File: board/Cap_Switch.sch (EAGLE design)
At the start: 9 parts, among them K1 TOS TLP241A, Q1 PN2222ABU, Q2 PN2222ABU

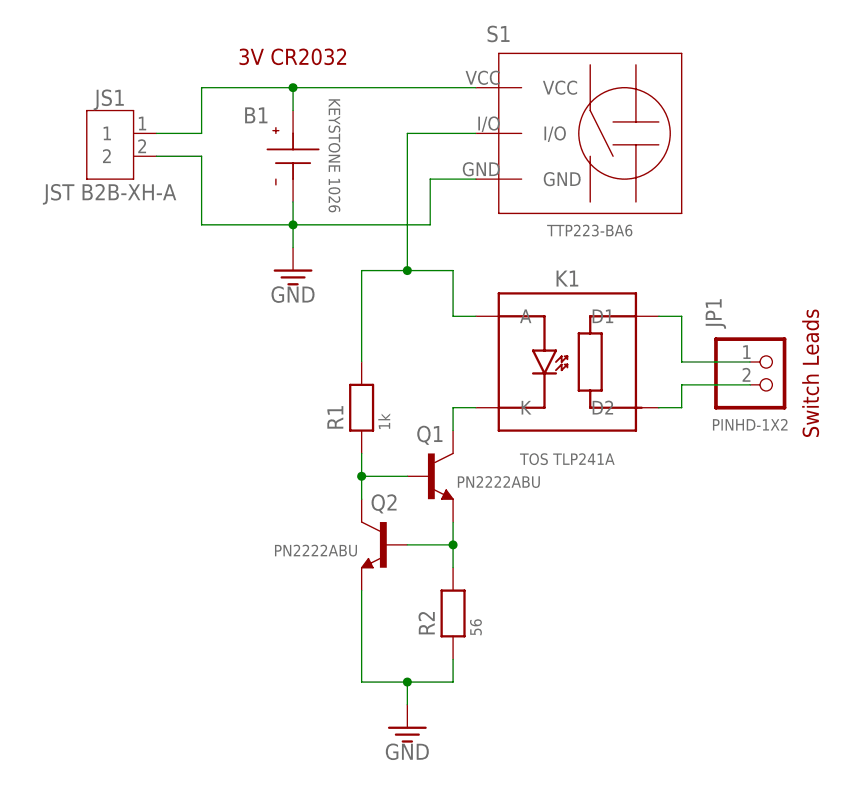
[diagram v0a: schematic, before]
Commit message: fixed coin cell polarity, new PH con
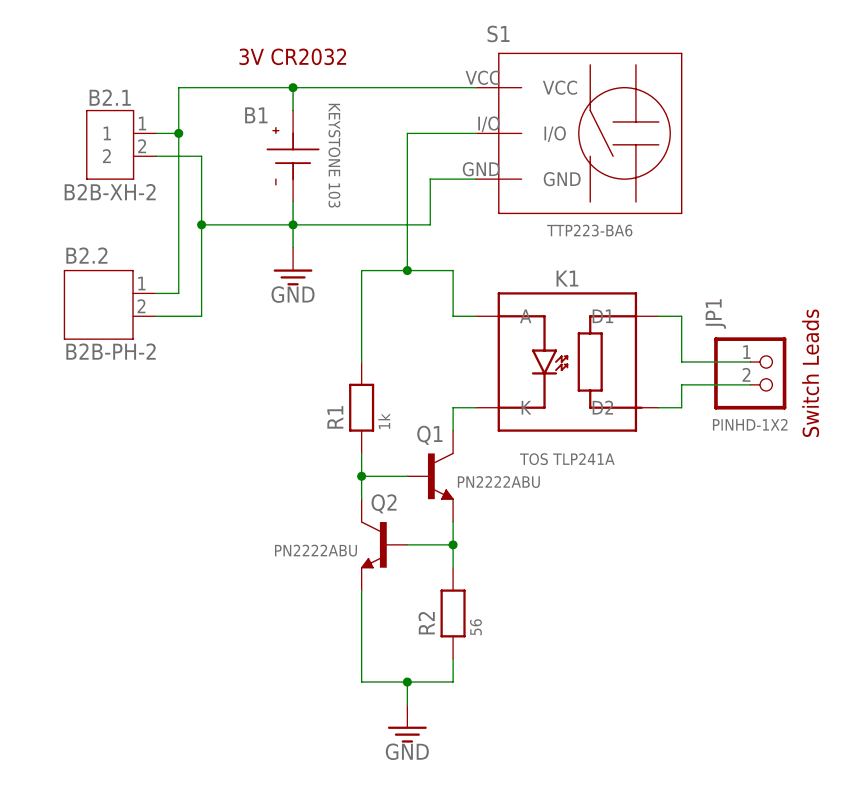
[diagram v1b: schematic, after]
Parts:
- added B2.2: B2B-PH-2, jst-ph:JST-PH2
- B1: value KEYSTONE 1026 -> KEYSTONE 103
- B2.1: value JST B2B-XH-A -> B2B-XH-2
- renumbered JS1 to B2.1
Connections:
- net GND: now also B1.NEG, B2.2.2; no longer B1.POSITIVE
- net V+: now also B1.POS, B2.2.1; no longer B1.NEGATIVE
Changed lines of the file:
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@@
 <layers>
 <layer number="1" name="Top" color="4" fill="1" visible="no" active="no"/>
-<layer number="2" name="Route2" color="1" fill="3" visible="no" active="no"/>
-<layer number="15" name="Route15" color="4" fill="6" visible="no" active="no"/>
+<layer number="2" name="Route2" color="16" fill="1" visible="no" active="no"/>
+<layer number="15" name="Route15" color="23" fill="1" visible="no" active="no"/>
 <layer number="16" name="Bottom" color="1" fill="1" visible="no" active="no"/>
 <layer number="17" name="Pads" color="2" fill="1" visible="no" active="no"/>
@@
 </classes>
 <parts>
-<part name="B1" library="home" deviceset="COINCELL-KEYSTONE#1026" device="" value="KEYSTONE 1026"/>
+<part name="B1" library="home" deviceset="COINCELL-KEYSTONE#1026" device="" value="KEYSTONE 103"/>
 <part name="R1" library="microbuilder" deviceset="RESISTOR" device="1206" value="1k"/>
 <part name="K1" library="home" deviceset="RELAY-SS-TOS-TLP241" device="-A" value="TOS TLP241A"/>
 <part name="JP1" library="Connector_writable" deviceset="PINHD-1X2" device="" package3d_urn="urn:adsk.eagle:package:22435/2"/>
 <part name="S1" library="home" deviceset="SWITCH-CAP-TOUCH" device="-AMZN" value="TTP223-BA6"/>
-<part name="JS1" library="Connector_writable" deviceset="B2B-XH-A" device="" package3d_urn="urn:adsk.eagle:package:24957641/6" value="JST B2B-XH-A"/>
+<part name="B2.1" library="Connector_writable" deviceset="B2B-XH-A" device="" package3d_urn="urn:adsk.eagle:package:24957641/6" value="B2B-XH-2"/>
 <part name="Q1" library="home" deviceset="BJT-NPN" device="-TO-92" value="PN2222ABU"/>
 <part name="R2" library="microbuilder" deviceset="RESISTOR" device="1206" value="56"/>
@@
 <part name="GND1" library="relay_box" deviceset="GND" device=""/>
 <part name="GND2" library="relay_box" deviceset="GND" device=""/>
+<part name="B2.2" library="jst-ph" deviceset="JST-PH2" device="" value="B2B-PH-2"/>
 </parts>
 <sheets>
@@
 <attribute name="VALUE" x="40.64" y="27.94" size="1.27" layer="96" ratio="10" rot="R180" align="bottom-center"/>
 </instance>
-<instance part="JS1" gate="G$1" x="-12.7" y="35.56" smashed="yes" rot="MR0">
+<instance part="B2.1" gate="G$1" x="-12.7" y="35.56" smashed="yes" rot="MR0">
 <attribute name="VALUE" x="-12.7" y="31.56" size="1.778" layer="96" rot="MR0" align="center"/>
 <attribute name="NAME" x="-12.7" y="42.06" size="1.778" layer="95" rot="MR0" align="center"/>
@@
 <instance part="GND2" gate="G$1" x="7.62" y="22.86" smashed="yes">
 <attribute name="VALUE" x="7.62" y="21.082" size="1.778" layer="96" align="top-center"/>
+</instance>
+<instance part="B2.2" gate="G$1" x="-15.24" y="20.32" smashed="yes">
+<attribute name="NAME" x="-17.78" y="23.622" size="1.778" layer="95"/>
+<attribute name="VALUE" x="-17.78" y="12.954" size="1.778" layer="96"/>
 </instance>
 </instances>
@@
 <wire x1="22.86" y1="33.02" x2="22.86" y2="27.94" width="0.1524" layer="91"/>
 <wire x1="22.86" y1="27.94" x2="7.62" y2="27.94" width="0.1524" layer="91"/>
-<pinref part="B1" gate="A" pin="POSITIVE"/>
+<pinref part="B1" gate="A" pin="NEG"/>
 <wire x1="7.62" y1="27.94" x2="7.62" y2="30.48" width="0.1524" layer="91"/>
 <wire x1="27.94" y1="33.02" x2="22.86" y2="33.02" width="0.1524" layer="91"/>
 <pinref part="S1" gate="A" pin="GND"/>
-<pinref part="JS1" gate="G$1" pin="2"/>
+<pinref part="B2.1" gate="G$1" pin="2"/>
 <wire x1="-7.55" y1="35.56" x2="-2.54" y2="35.56" width="0.1524" layer="91"/>
 <wire x1="-2.54" y1="35.56" x2="-2.54" y2="27.94" width="0.1524" layer="91"/>
@@
 <pinref part="GND2" gate="G$1" pin="GND"/>
 <wire x1="7.62" y1="27.94" x2="7.62" y2="25.4" width="0.1524" layer="91"/>
+<pinref part="B2.2" gate="G$1" pin="2"/>
+<wire x1="-7.62" y1="17.78" x2="-2.54" y2="17.78" width="0.1524" layer="91"/>
+<wire x1="-2.54" y1="17.78" x2="-2.54" y2="27.94" width="0.1524" layer="91"/>
+<junction x="-2.54" y="27.94"/>
 </segment>
 </net>
 <net name="V+" class="1">
 <segment>
-<pinref part="B1" gate="A" pin="NEGATIVE"/>
+<pinref part="B1" gate="A" pin="POS"/>
 <wire x1="7.62" y1="40.64" x2="7.62" y2="43.18" width="0.1524" layer="91"/>
 <wire x1="27.94" y1="43.18" x2="7.62" y2="43.18" width="0.1524" layer="91"/>
 <pinref part="S1" gate="A" pin="VCC"/>
-<pinref part="JS1" gate="G$1" pin="1"/>
-<wire x1="-7.55" y1="38.1" x2="-2.54" y2="38.1" width="0.1524" layer="91"/>
-<wire x1="-2.54" y1="38.1" x2="-2.54" y2="43.18" width="0.1524" layer="91"/>
-<wire x1="-2.54" y1="43.18" x2="7.62" y2="43.18" width="0.1524" layer="91"/>
+<pinref part="B2.1" gate="G$1" pin="1"/>
+<wire x1="-7.55" y1="38.1" x2="-5.08" y2="38.1" width="0.1524" layer="91"/>
+<wire x1="-5.08" y1="43.18" x2="7.62" y2="43.18" width="0.1524" layer="91"/>
 <junction x="7.62" y="43.18"/>
+<pinref part="B2.2" gate="G$1" pin="1"/>
+<wire x1="-7.62" y1="20.32" x2="-5.08" y2="20.32" width="0.1524" layer="91"/>
+<wire x1="-5.08" y1="20.32" x2="-5.08" y2="38.1" width="0.1524" layer="91"/>
+<junction x="-5.08" y="38.1"/>
+<wire x1="-5.08" y1="43.18" x2="-5.08" y2="38.1" width="0.1524" layer="91"/>
 </segment>
 </net>
